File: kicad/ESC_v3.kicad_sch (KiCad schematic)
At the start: 26 parts, among them J1 Conn_01x05_Pin, J2 Conn_01x05_Pin, J4 Conn_01x06_Pin, J5 Conn_01x02_Pin, J6 Conn_01x06_Pin, J7 Conn_01x02_Pin, J8 Conn_01x04_Pin, SW2 SW_Nidec_CAS-120A1, U1 STSPIN32G4, U10 BD4104, U14 MCP9700x-ETT

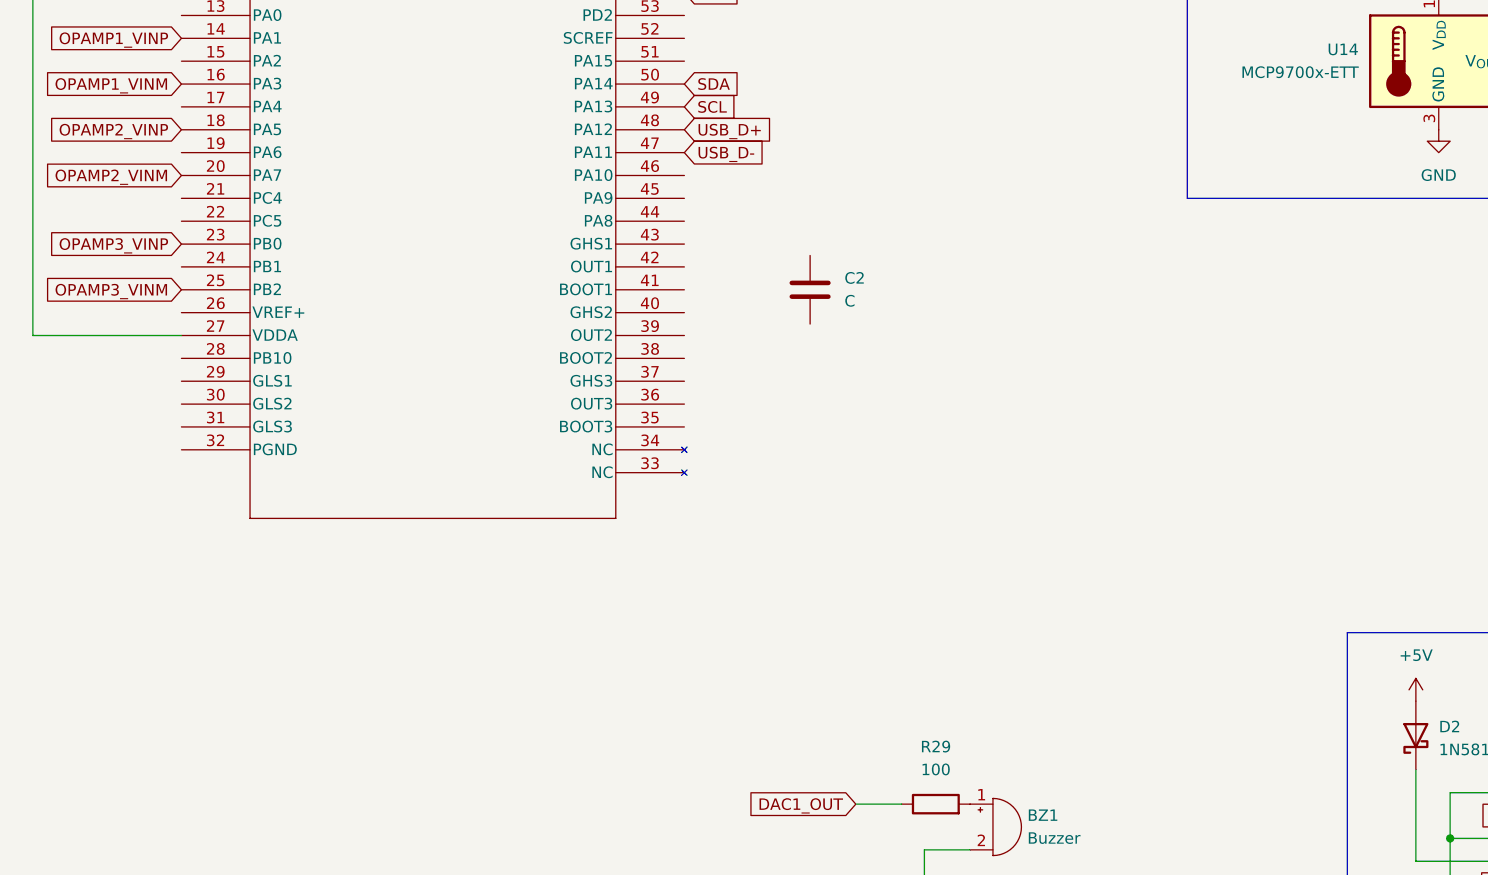
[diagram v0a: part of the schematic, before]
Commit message: add .ioc to v2_mini branch and setting STM32G431VBx3 for STSPIN32G4
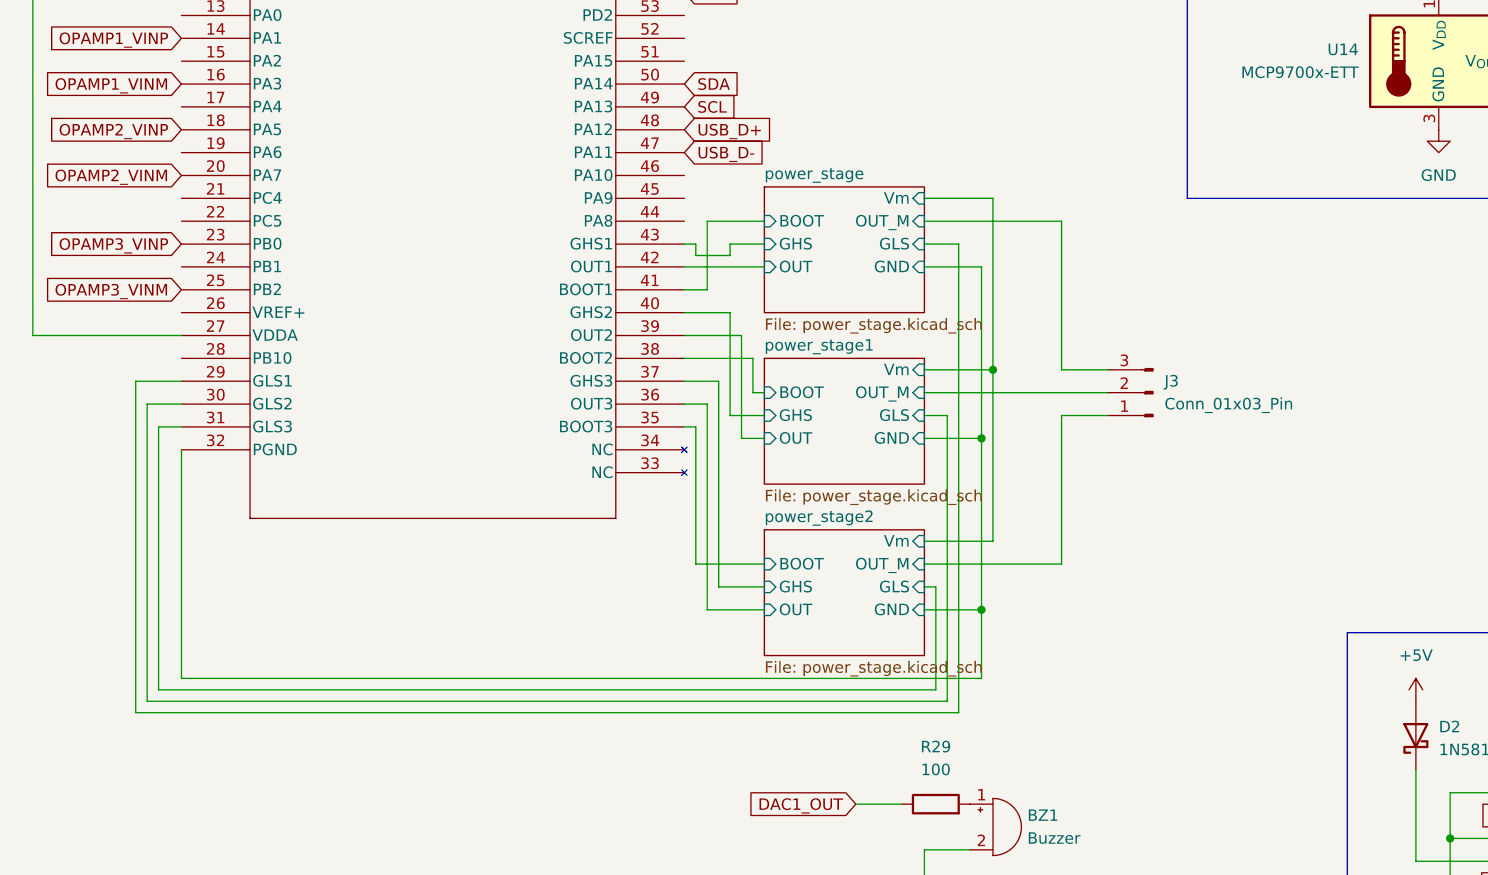
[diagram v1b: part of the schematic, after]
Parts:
- removed C2: C, symbol Device:C
- added J3: Conn_01x03_Pin, symbol Connector:Conn_01x03_Pin
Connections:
- net power_stage/GLS: now reaches U1.29 (GLS1)
- net power_stage1/GLS: now reaches U1.30 (GLS2)
- net power_stage2/GLS: now reaches U1.31 (GLS3)
- net power_stage/GND: now reaches U1.32 (PGND)
- net power_stage2/BOOT: now reaches U1.35 (BOOT3)
- net power_stage2/OUT: now reaches U1.36 (OUT3)
- net power_stage2/GHS: now reaches U1.37 (GHS3)
- net power_stage1/BOOT: now reaches U1.38 (BOOT2)
- net power_stage1/OUT: now reaches U1.39 (OUT2)
- net power_stage1/GHS: now reaches U1.40 (GHS2)
- net power_stage/BOOT: now reaches U1.41 (BOOT1)
- net power_stage/OUT: now reaches U1.42 (OUT1)
- net power_stage/GHS: now reaches U1.43 (GHS1)
- new net power_stage/OUT_M: J3.3 (Pin_3)
- new net power_stage1/OUT_M: J3.2 (Pin_2)
- new net power_stage2/OUT_M: J3.1 (Pin_1)
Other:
- added sheet power_stage (power_stage.kicad_sch)
- added sheet power_stage1 (power_stage.kicad_sch)
- added sheet power_stage2 (power_stage.kicad_sch)

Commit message: a
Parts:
- removed BZ1: Buzzer, jisaku:buzzer_unified, symbol Device:Buzzer
- removed J1: Conn_01x05_Pin, Connector_JST:JST_XH_S5B-XH-A_1x05_P2.50mm_Horizontal, symbol Connector:Conn_01x05_Pin
- removed J4: Conn_01x06_Pin, Connector_JST:JST_PH_B6B-PH-K_1x06_P2.00mm_Vertical, symbol Connector:Conn_01x06_Pin
- removed R29: 100, Resistor_SMD:R_0402_1005Metric_Pad0.72x0.64mm_HandSolder, symbol Device:R
- added BZ2: Buzzer, jisaku:buzzer_unified, symbol Device:Buzzer
- added J1: Conn_01x07, Connector_JST:JST_GH_SM07B-GHS-TB_1x07-1MP_P1.25mm_Horizontal, symbol Connector_Generic:Conn_01x07
- added J4: Conn_01x04, Connector_JST:JST_GH_SM04B-GHS-TB_1x04-1MP_P1.25mm_Horizontal, symbol Connector_Generic:Conn_01x04
- added JP1: SolderJumper_3_Bridged12, symbol Jumper:SolderJumper_3_Bridged12
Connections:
- net SCL is gone; now on net I2C_SCL: U1.49 (PA13)
- net SDA is gone; now on net I2C_SDA: U1.50 (PA14)
- net TIM2_CH1 is gone; now on net CH1: J2.2 (Pin_2)
- net TIM2_CH2 is gone; now on net CH2: J2.3 (Pin_3)
- net TIM2_CH3 is gone; now on net CH3: J2.4 (Pin_4)
- net +3.3V: now also J1.1 (Pin_1), J4.1 (Pin_1), JP1.3 (B)
- net +5V: now also JP1.1 (A); no longer J2.1 (Pin_1)
- net GND: now also BZ2.2 (-), J1.3 (Pin_3), J4.3 (Pin_3)
- net RX: now also U1.22 (PC5)
- net TX: now also U1.21 (PC4)
- net ADC1_IN7: now reaches U1.10 (PC1)
- net ADC1_IN7: now also J1.4 (Pin_4), J4.4 (Pin_4)
- net ADC1_IN8: now reaches U1.11 (PC2)
- net ADC1_IN8: now also J1.2 (Pin_2), J4.2 (Pin_2)
- net ADC1_IN9: now reaches U1.12 (PC3)
- net DAC1_OUT1: now reaches U1.17 (PA4)
- new net: J2.1 (Pin_1), JP1.2 (C)
- new net Untitled Sheet/OUT: BZ2.1 (+)
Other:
- added sheet Untitled Sheet (spk.kicad_sch)
- sheet power_stage ports: added OPAMP_M, OPAMP_P; removed none
- sheet power_stage1 ports: added OPAMP_M, OPAMP_P; removed none
- sheet power_stage2 ports: added OPAMP_M, OPAMP_P; removed none
- moved on the sheet: J3, U14

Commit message: w
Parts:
- removed J3: Conn_01x03_Pin, symbol Connector:Conn_01x03_Pin
- added C3: C, symbol Device:C
- added J10: Conn_01x03, symbol Connector_Generic:Conn_01x03
- added J9: Conn_01x02, symbol Connector_Generic:Conn_01x02
- added R12, R13, R14, R15, R16, R17, R2: R, symbol Device:R
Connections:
- net ADC1_IN1 is gone; now on net ADC1_IN9: U14.2 (V_{OUT})
- net power_stage/GND is gone; now on net GNDPWR: U1.32 (PGND)
- net +15V: now also C3.1, J9.1 (Pin_1)
- net +3.3V: now also R13.2, R16.2
- net +5V: now also U1.64 (REGIN)
- net GND: now also R14.1, R17.1
- net OPAMP1_VINP: now also R12.2, R13.1, R14.2
- net OPAMP2_VINP: now also R15.2, R16.1, R17.2
- net OPAMP3_VINP: now also J9.2 (Pin_2), R2.2
- net power_stage/OUT_M: now also J10.1 (Pin_1)
- net power_stage1/OUT_M: now also J10.2 (Pin_2)
- net power_stage2/OUT_M: now also J10.3 (Pin_3)
- net RCC_HSE: now reaches U1.6 (PF0)
- net OPAMP3_VINM renamed GNDPWR
- net GNDPWR: now also C3.2, R2.1
- new net power_stage/OPAMP_P: R12.1
- new net power_stage1/OPAMP_P: R15.1

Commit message: a
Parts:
- added C6, C7, C8: 10u, Capacitor_SMD:C_0402_1005Metric, symbol Device:C
- C1: value C -> 10u; footprint (none) -> Capacitor_SMD:C_0402_1005Metric
- C3: value C -> 470u; footprint (none) -> Capacitor_SMD:C_Elec_10x10.2
- D1: footprint (none) -> Diode_SMD:D_SOD-323_HandSoldering
- J10: footprint (none) -> Connector_AMASS:AMASS_MR30PW-FB_1x03_P3.50mm_Horizontal
- J9: footprint (none) -> Connector_AMASS:AMASS_XT30PW-M_1x02_P2.50mm_Horizontal
- JP1: footprint (none) -> Jumper:SolderJumper-3_P1.3mm_Bridged12_Pad1.0x1.5mm
- L1: value L -> 10uH; footprint (none) -> Inductor_SMD:L_1210_3225Metric; Field5 (none) -> FTC322520S220MBCA
- R12, R13, R14, R15, R16, R17: footprint (none) -> Resistor_SMD:R_0402_1005Metric_Pad0.72x0.64mm_HandSolder
- U1: footprint QFN_IN32G4_STM -> stspin32g4:QFN_IN32G4_STM
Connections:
- net +5V: now also C7.1
- net GND: now also C6.2, C7.2, C8.2
- net at U1.1 (REG3V3/VDD), U1.2 (VBAT), U1.27 (VDDA): now also C6.1
- net at C1.1, L1.2, U1.63 (VCC): now also C8.1

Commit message: a
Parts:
- removed J5: Conn_01x02_Pin, Connector_PinHeader_2.54mm:PinHeader_1x02_P2.54mm_Vertical, symbol Connector:Conn_01x02_Pin
- added C10, C11: 10u, Capacitor_SMD:C_0402_1005Metric, symbol Device:C
- added C9: 22u, Capacitor_SMD:C_0603_1608Metric, symbol Device:C
- added D3: 1N4148WT, Diode_SMD:D_SOD-523, symbol Diode:1N4148WT
- added D4: LED_B, LED_SMD:LED_0603_1608Metric, symbol Device:LED
- added D5, D9: LED_G, LED_SMD:LED_0603_1608Metric, symbol Device:LED
- added D6, D8: LED_R, LED_SMD:LED_0603_1608Metric, symbol Device:LED
- added D7: D, Diode_SMD:D_SOD-323_HandSoldering, symbol Device:D
- added J3: USB_C_Receptacle_USB2.0, Connector_USB:USB_C_Receptacle_GCT_USB4105-xx-A_16P_TopMnt_Horizontal, symbol Connector:USB_C_Receptacle_USB2.0
- added JP2: SolderJumper_2_Open, Jumper:SolderJumper-2_P1.3mm_Open_RoundedPad1.0x1.5mm, symbol Jumper:SolderJumper_2_Open
- added L2: L, Inductor_SMD:L_0402_1005Metric, symbol Device:L
- added R11, R8: R, Resistor_SMD:R_2010_5025Metric_Pad1.40x2.65mm_HandSolder, symbol Device:R
- added R18, R19, R20: R, Resistor_SMD:R_0402_1005Metric_Pad0.72x0.64mm_HandSolder, symbol Device:R
- added R21, R22, R25, R26, R29: 2.2k, Resistor_SMD:R_0402_1005Metric_Pad0.72x0.64mm_HandSolder, symbol Device:R
- added R23, R24: 5.1k, Resistor_SMD:R_0603_1608Metric, symbol Device:R
- added U2: AMS1117-5.0, Package_TO_SOT_SMD:SOT-223-3_TabPin2, symbol Regulator_Linear:AMS1117-5.0
- added X1: IQXO-70, Oscillator:Oscillator_SMD_IQD_IQXO70-4Pin_7.5x5.0mm, symbol Oscillator:IQXO-70
- J10: footprint Connector_AMASS:AMASS_MR30PW-FB_1x03_P3.50mm_Horizontal -> jisaku:MR30_side_SMD
- J2: footprint Connector_JST:JST_XH_S5B-XH-A_1x05_P2.50mm_Horizontal -> Connector_JST:JST_XH_B5B-XH-A_1x05_P2.50mm_Vertical
- J7: footprint Connector_JST:JST_XH_S2B-XH-A_1x02_P2.50mm_Horizontal -> Connector_JST:JST_XH_B2B-XH-A_1x02_P2.50mm_Vertical
- R2: footprint (none) -> Resistor_SMD:R_2010_5025Metric_Pad1.40x2.65mm_HandSolder
- SW2: footprint Connector_PinHeader_2.54mm:PinHeader_1x03_P2.54mm_Vertical -> Button_Switch_SMD:SW_DPDT_CK_JS202011JCQN
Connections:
- net OPAMP1_VINM is gone; now on net GNDPWR: U1.16 (PA3)
- net OPAMP2_VINM is gone; now on net OPAMP1_VINP: U1.20 (PA7)
- net +15V: now also J9.2 (Pin_2), C10.1, U2.3 (VI); no longer J9.1 (Pin_1)
- net +3.3V: now also C6.1, U1.2 (VBAT), U1.27 (VDDA), D7.1 (K), L2.1, R19.2, X1.4 (V+)
- net +5V: now also C9.1, D3.1 (K), U2.2 (VO)
- net CAN_H: now also JP2.2 (B)
- net CAN_RX: now also D8.2 (A)
- net CAN_TX: now also D9.2 (A)
- net CLK: now also U1.50 (PA14)
- net DAC1_OUT1: now also U1.52 (SCREF), C11.1
- net DIO: now also U1.49 (PA13)
- net GND: now also C11.2, D4.1 (K), D5.1 (K), D6.1 (K), J3.A1 (GND), J3.A12 (GND), J3.B1 (GND), J3.B12 (GND), J3.S1 (SHIELD), R20.1, R23.2, R24.2, R26.1, R29.1, X1.2 (GND)
- net GNDPWR: now also U1.18 (PA5), R11.2, R18.1, R8.2; no longer U1.25 (PB2)
- net I2C_SCL: now also U1.21 (PC4); no longer U1.49 (PA13)
- net I2C_SDA: now also U1.44 (PA8); no longer U1.50 (PA14)
- net OPAMP1_VINP: no longer U1.14 (PA1)
- net OPAMP2_VINP: now also U1.23 (PB0); no longer U1.18 (PA5)
- net OPAMP3_VINP: now also U1.14 (PA1), R18.2, R19.1, R20.2; no longer J9.2 (Pin_2), R2.2, U1.23 (PB0)
- net RCC_HSE: now also X1.3 (OUT)
- net RX: now also U1.46 (PA10); no longer U1.22 (PC5)
- net TIM4_CH2: now also U1.57 (PB6); no longer U1.58 (PB7)
- net TX: now also U1.45 (PA9); no longer U1.21 (PC4)
- net ToggleSwitch: now also U1.51 (PA15)
- net USB_D+: now also J3.A6 (D+), J3.B6 (D+)
- net USB_D-: now also J3.A7 (D-), J3.B7 (D-)
- net at R43.2: now also JP2.1 (A)
- net at U1.26 (VREF+): now also L2.2
- net at U1.3 (PC13): now also R25.2
- net at U1.4 (PC14): now also R22.2
- net at U1.5 (PC15): now also R21.2
- net power_stage/OPAMP_P renamed power_stage/GND
- net power_stage/GND: now also R8.1
- net power_stage1/OPAMP_P renamed power_stage1/GND
- net power_stage1/GND: now also R11.1
- new net: D5.2 (A), R22.1
- new net: D8.1 (K), R26.2
- new net: D3.2 (A), J3.A4 (VBUS), J3.A9 (VBUS), J3.B4 (VBUS), J3.B9 (VBUS)
- new net: J3.A5 (CC1), R23.1
- new net: J3.B5 (CC2), R24.1
- new net: D9.1 (K), R29.2
- new net: D6.2 (A), R21.1
- new net: D7.2 (A), U1.1 (REG3V3/VDD)
- new net: D4.2 (A), R25.1
- new net OPAMP3_VINM: C10.2, C9.2, J9.1 (Pin_1), R2.2, U1.25 (PB2), U2.1 (GND)
- no-connect marks 0 -> 2
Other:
- sheet power_stage ports: added none; removed OPAMP_M, OPAMP_P
- sheet power_stage1 ports: added none; removed OPAMP_M, OPAMP_P
- sheet power_stage2 ports: added none; removed OPAMP_M, OPAMP_P
- moved on the sheet: C6, J9, R12, R13, R14, R15, R16, R17

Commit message: finish
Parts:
- removed BZ2: Buzzer, jisaku:buzzer_unified, symbol Device:Buzzer
- added D10, D11, D12: LED_R, LED_SMD:LED_0603_1608Metric, symbol Device:LED
- added JP3, JP4: SolderJumper_2_Open, Jumper:SolderJumper-2_P1.3mm_Open_RoundedPad1.0x1.5mm, symbol Jumper:SolderJumper_2_Open
- added R27, R31, R32, R33: 22k, Resistor_SMD:R_0402_1005Metric_Pad0.72x0.64mm_HandSolder, symbol Device:R
- added R28: 4.7k, Resistor_SMD:R_0402_1005Metric_Pad0.72x0.64mm_HandSolder, symbol Device:R
- added R30: 2.2k, Resistor_SMD:R_0402_1005Metric_Pad0.72x0.64mm_HandSolder, symbol Device:R
- added TP1, TP2, TP3, TP4: TestPoint, TestPoint:TestPoint_Pad_D1.5mm, symbol Connector:TestPoint
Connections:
- net OPAMP3_VINM is gone; now on net GND: C10.2, C9.2, J9.1 (Pin_1), R2.2, U1.25 (PB2), U2.1 (GND)
- net +15V: now also D10.2 (A)
- net +3.3V: now also D12.2 (A), JP4.1 (A)
- net +5V: now also D11.2 (A)
- net CH1: now also R31.2
- net CH2: now also R32.2
- net CH3: now also R33.2
- net GND: now also R28.1, R30.1, TP4.1
- net GNDPWR: now also R27.1
- net USB_D+: now also TP3.1
- net USB_D-: now also TP2.1
- net button: now also U1.9 (PC0)
- net at D3.2 (A), J3.A4 (VBUS), J3.A9 (VBUS)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: now also TP1.1
- net at J2.1 (Pin_1), JP1.2 (C): now also JP3.2 (B)
- net at U10.5 (SPLIT): now also JP4.2 (B)
- new net: D10.1 (K), R27.2
- new net: D11.1 (K), R28.2
- new net: D12.1 (K), R30.2
- new net: JP3.1 (A), R31.1, R32.1, R33.1
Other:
- removed sheet Untitled Sheet

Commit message: order finished
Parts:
- C1, C10, C8: footprint Capacitor_SMD:C_0402_1005Metric -> Capacitor_SMD:C_0603_1608Metric
- D1, D7: value D -> 1N5819WS
- D2: footprint Diode_SMD:D_SOD-323 -> Diode_SMD:D_SOD-323_HandSoldering
- D3: value 1N4148WT -> 1N5819WS; footprint Diode_SMD:D_SOD-523 -> Diode_SMD:D_SOD-323_HandSoldering
- L1: value 10uH -> 22uH
- R11, R2, R8: value R -> 5m
- R12, R15, R18: value R -> 1k
- R13, R14, R16, R17, R19, R20: value R -> 33k
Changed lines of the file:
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@@
 			)
 		)
-		(property "Value" "R"
+		(property "Value" "33k"
 			(at 73.66 194.3099 0)
 			(effects
@@
 			)
 		)
-		(property "Footprint" "Capacitor_SMD:C_0402_1005Metric"
+		(property "Footprint" "Capacitor_SMD:C_0603_1608Metric"
 			(at 46.6852 189.23 0)
 			(effects
@@
 			)
 		)
-		(property "Value" "R"
+		(property "Value" "5m"
 			(at 124.46 100.33 90)
 			(effects
@@
 			)
 		)
-		(property "Value" "R"
+		(property "Value" "1k"
 			(at 67.31 185.42 90)
 			(effects
@@
 			)
 		)
-		(property "Value" "R"
+		(property "Value" "1k"
 			(at 134.62 77.47 90)
 			(effects
@@
 			)
 		)
-		(property "Value" "D"
+		(property "Value" "1N5819WS"
 			(at 110.49 40.6399 90)
 			(effects
@@
 			)
 		)
-		(property "Value" "R"
+		(property "Value" "1k"
 			(at 142.24 97.79 90)
 			(effects
@@
 			)
 		)
-		(property "Value" "R"
+		(property "Value" "33k"
 			(at 73.66 186.6899 0)
 			(effects
@@
 			)
 		)
-		(property "Value" "R"
+		(property "Value" "33k"
 			(at 140.97 78.7399 0)
 			(effects
@@
 			)
 		)
-		(property "Value" "R"
+		(property "Value" "33k"
 			(at 148.59 99.0599 0)
 			(effects
@@
 			)
 		)
-		(property "Footprint" "Capacitor_SMD:C_0402_1005Metric"
+		(property "Footprint" "Capacitor_SMD:C_0603_1608Metric"
 			(at 126.6952 43.18 0)
 			(effects
@@
 			)
 		)
-		(property "Footprint" "Capacitor_SMD:C_0402_1005Metric"
+		(property "Footprint" "Capacitor_SMD:C_0603_1608Metric"
 			(at 116.5352 43.18 0)
 			(effects
@@
 			)
 		)
-		(property "Value" "R"
+		(property "Value" "5m"
 			(at 40.64 180.34 90)
 			(effects
@@
 			)
 		)
-		(property "Value" "D"
+		(property "Value" "1N5819WS"
 			(at 27.94 24.13 0)
 			(effects
@@
 			)
 		)
-		(property "Value" "R"
+		(property "Value" "5m"
 			(at 124.46 80.01 90)
 			(effects
@@
 			)
 		)
-		(property "Footprint" "Diode_SMD:D_SOD-323"
+		(property "Footprint" "Diode_SMD:D_SOD-323_HandSoldering"
 			(at 173.355 138.43 0)
 			(effects
@@
 			)
 		)
-		(property "Value" "10uH"
+		(property "Value" "22uH"
 			(at 111.76 33.02 90)
 			(effects
@@
 			)
 		)
-		(property "Value" "R"
+		(property "Value" "33k"
 			(at 140.97 86.3599 0)
 			(effects
@@
 			)
 		)
-		(property "Value" "1N4148WT"
+		(property "Value" "1N5819WS"
 			(at 120.65 144.78 0)
 			(effects
@@
 			)
 		)
-		(property "Footprint" "Diode_SMD:D_SOD-523"
+		(property "Footprint" "Diode_SMD:D_SOD-323_HandSoldering"
 			(at 120.65 144.145 0)
 			(effects
@@
 			)
 		)
-		(property "Value" "R"
+		(property "Value" "33k"
 			(at 148.59 106.6799 0)
 			(effects

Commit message: a
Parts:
- added R34: 10k, Resistor_SMD:R_0402_1005Metric_Pad0.72x0.64mm_HandSolder, symbol Device:R
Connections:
- net +3.3V: now also R34.2
- net TMP: now reaches U1.7 (PF1)
- net TMP: now also J1.5 (Pin_5), R34.1
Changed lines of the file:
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@@
 	)
 	(junction
+		(at 190.5 52.07)
+		(diameter 0)
+		(color 0 0 0 0)
+	)
+	(junction
 		(at 278.13 156.21)
 		(diameter 0)
@@
 	)
 	(junction
+		(at 181.61 41.91)
+		(diameter 0)
+		(color 0 0 0 0)
+	)
+	(junction
 		(at 267.97 140.97)
 		(diameter 0)
@@
 	(wire
 		(pts
+			(xy 190.5 52.07) (xy 193.04 52.07)
+		)
+		(stroke
+			(width 0)
+			(type default)
+		)
+	)
+	(wire
+		(pts
 			(xy 64.77 177.8) (xy 64.77 181.61)
 		)
@@
 	(wire
 		(pts
+			(xy 173.99 52.07) (xy 190.5 52.07)
+		)
+		(stroke
+			(width 0)
+			(type default)
+		)
+	)
+	(wire
+		(pts
 			(xy 91.44 13.97) (xy 93.98 13.97)
 		)
@@
 	(wire
 		(pts
+			(xy 190.5 44.45) (xy 190.5 41.91)
+		)
+		(stroke
+			(width 0)
+			(type default)
+		)
+	)
+	(wire
+		(pts
 			(xy 92.71 83.82) (xy 96.52 83.82)
 		)
@@
 	(wire
 		(pts
+			(xy 190.5 41.91) (xy 181.61 41.91)
+		)
+		(stroke
+			(width 0)
+			(type default)
+		)
+	)
+	(wire
+		(pts
 			(xy 116.84 134.62) (xy 116.84 101.6)
 		)
@@
 		)
 	)
+	(global_label "TMP"
+		(shape input)
+		(at 193.04 52.07 0)
+		(fields_autoplaced yes)
+		(effects
+			(font
+				(size 1.27 1.27)
+			)
+			(justify left)
+		)
+		(property "Intersheetrefs" "${INTERSHEET_REFS}"
+			(at 199.7142 52.07 0)
+			(effects
+				(font
+					(size 1.27 1.27)
+				)
+				(justify left)
+				(hide yes)
+			)
+		)
+	)
 	(global_label "CAN_RX"
 		(shape input)
@@
 		)
 	)
+	(global_label "TMP"
+		(shape input)
+		(at 31.75 43.18 180)
+		(fields_autoplaced yes)
+		(effects
+			(font
+				(size 1.27 1.27)
+			)
+			(justify right)
+		)
+		(property "Intersheetrefs" "${INTERSHEET_REFS}"
+			(at 25.0758 43.18 0)
+			(effects
+				(font
+					(size 1.27 1.27)
+				)
+				(justify right)
+				(hide yes)
+			)
+		)
+	)
 	(global_label "OPAMP2_VINM"
 		(shape input)
@@
 					(unit 1)
 				)
+			)
+		)
+	)
+	(symbol
+		(lib_id "Device:R")
+		(at 190.5 48.26 180)
+		(unit 1)
+		(exclude_from_sim no)
+		(in_bom yes)
+		(on_board yes)
+		(dnp no)
+		(fields_autoplaced yes)
+		(property "Reference" "R34"
+			(at 193.04 46.9899 0)
+			(effects
+				(font
+					(size 1.27 1.27)
+				)
+				(justify right)
+			)
+		)
+		(property "Value" "10k"
+			(at 193.04 49.5299 0)
+			(effects
+				(font
+					(size 1.27 1.27)
+				)
+				(justify right)
+			)
+		)
+		(property "Footprint" "Resistor_SMD:R_0402_1005Metric_Pad0.72x0.64mm_HandSolder"
+			(at 192.278 48.26 90)
+			(effects
+				(font
+					(size 1.27 1.27)
+				)
+				(hide yes)
+			)
+		)
+		(property "Datasheet" "~"
+			(at 190.5 48.26 0)
+			(effects
+				(font
+					(size 1.27 1.27)
+				)
+				(hide yes)
+			)
+		)
+		(property "Description" "Resistor"
+			(at 190.5 48.26 0)
+			(effects
+				(font
+					(size 1.27 1.27)
+				)
+				(hide yes)
+			)
+		)
+		(property "LCSC" "C25744"
+			(at 184.15 48.26 0)
+			(effects
+				(font
+					(size 1.27 1.27)
+				)
+				(hide yes)
+			)
+		)
+		(pin "2"
+		)
+		(pin "1"
+		)
+		(instances
+			(project "ESC_v3"
+				(path "/643a74e6-da9a-4f0e-bb82-8f2ac15e39e7"
+					(reference "R34")
+					(unit 1)
+				)
